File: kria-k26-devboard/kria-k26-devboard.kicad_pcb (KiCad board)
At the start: 8 copper layers, 121.5 x 89.8 mm, 397 parts, among them IC1 TPS2378DDA, IC2 USB5534B-5000JZX, J1 5-2337992-8, J2 USB4105-GF-A, J3 DC_SOCKET, J4 WE_68715014522, J5 47272-0001, J6 1140084168, J7 0878311420, J8 SSW-106-02-G-D-RA, M1 XILINX-KRIA-K26, P1 2199119-6, Q1 BSS138DW-7-F, Q2 PJA3441, Q3 BSS123, Q4 AO3401A, Q5 BSS138-7-F, Q6 BSS138-7-F, Q7 BSS138-7-F, Q8 BSS138-7-F, U1 DP83867CRRGZR, U10 AP62301WU-7, U11 AP62301WU-7, U12 LTC4358CDE, U13 LTC4358CDE, U14 LTC4358CDE, U15 USB3310C-CP, U16 TPD4E05U06QDQARQ1, U17 TPD4E05U06QDQARQ1, U18 GSB3112311HR, U19 TPD4E05U06QDQARQ1, U2 MAX5984AETI+T, U20 TPD4E05U06QDQARQ1, U21 GSB3112311HR, U22 PI4MSD5V9540BUEX, U23 FT4232HPQ, U24 SN74AVC4T245PWR, U25 FIN1019MTC, U26 TPD4E05U06QDQARQ1, U27 NVT4858HKZ, U28 TPS2116DRLR, U29 SN74AVC4T245PWR, U3 AP62301WU-7, U30 SN74AVC4T245PWR, U31 TPS3840PH30DBVR, U32 TPS3840PH30DBVR, U33 74LV07ATPWJ, U34 AP62301WU-7, U35 93LC56CT-IMC, U36 SN74AVC2T245RSWR, U37 SN74AVC2T245RSWR, U38 SN74AVC4T245PWR, U39 SN74AVC4T245PWR, U4 AP62301WU-7, U40 NC7WZ07P6X, U41 PCA9306D_118, U42 M24C64-FMC6TG, U43 TPD4E05U06QDQARQ1, U44 TPD4E05U06QDQARQ1, U5 AP62301WU-7, U6 AP62301WU-7, U7 AP62301WU-7, U8 RPX-4.0-R, U9 AP62301WU-7, Y1 ABM8G-25.000MHZ-18-D2Y-T, Y2 ABM8G-12.000MHZ-18-D2Y-T

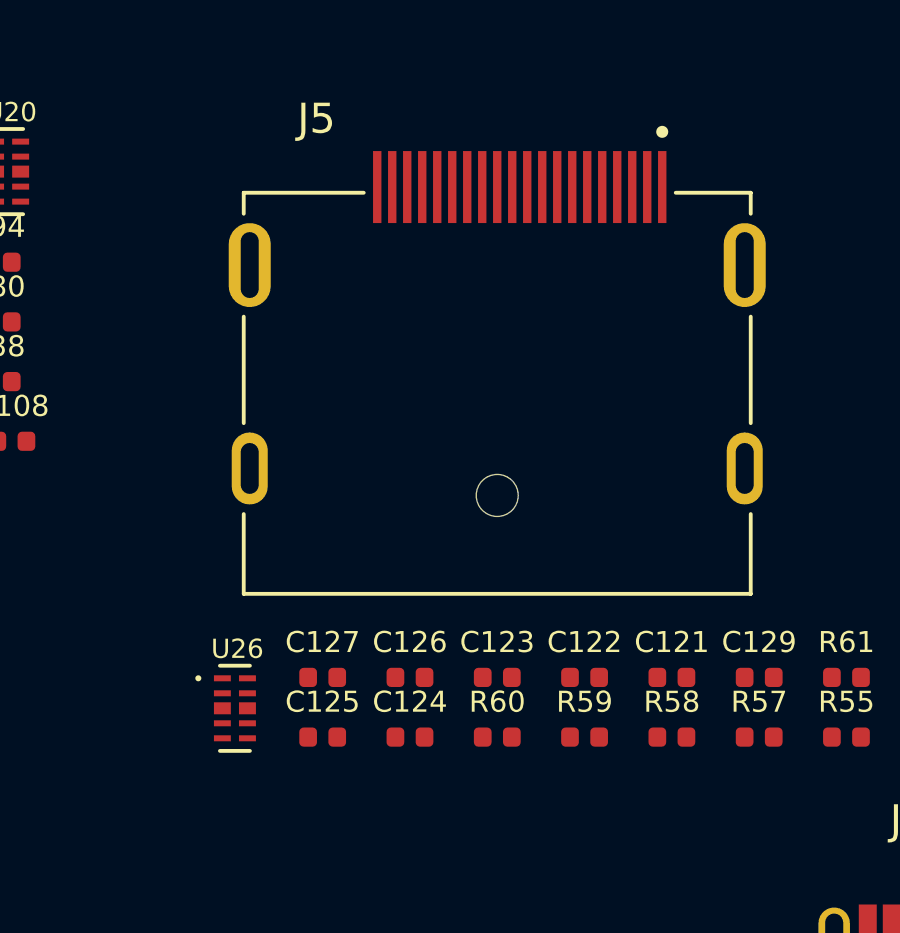
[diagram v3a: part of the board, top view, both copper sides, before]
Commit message: Added Led voltage indicator, fan circuit. Tidied up supply and SOM sheet
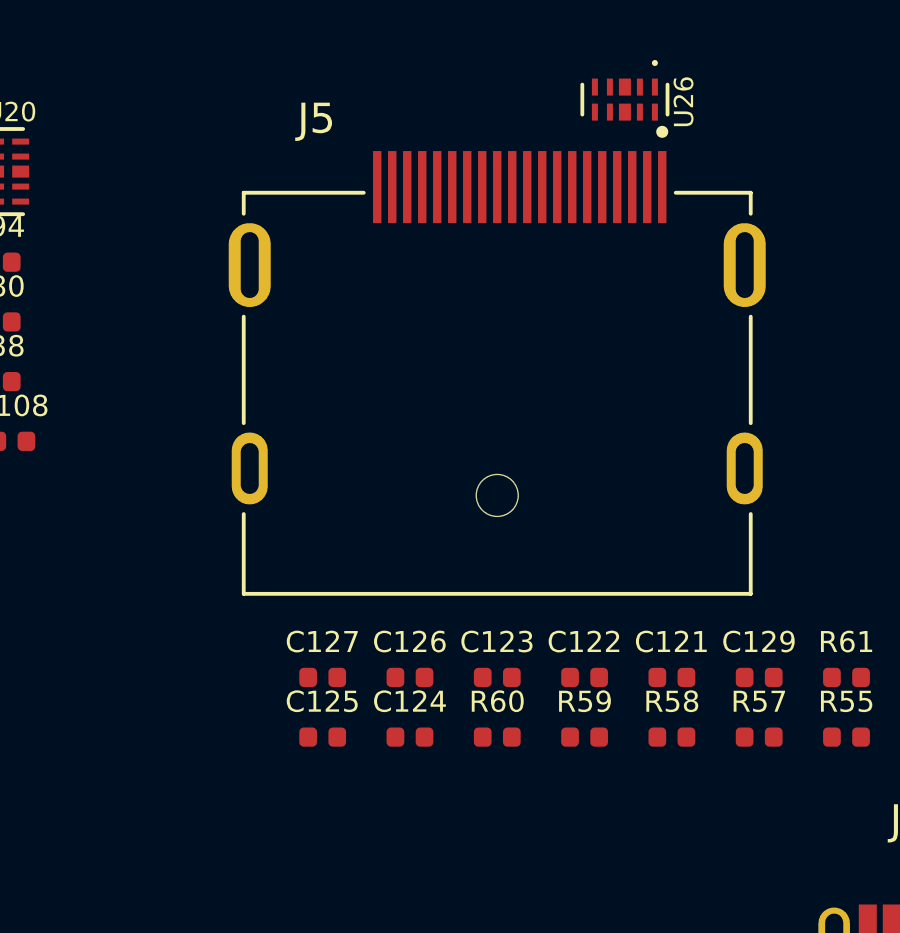
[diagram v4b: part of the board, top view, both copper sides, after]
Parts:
- moved U26 24.1 mm to (205.3, -118.8), turned to 270 degrees

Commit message: Initial placement of power supply
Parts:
- removed L9: PFL1609-102MEW, antmicro-footprints:0603-res
- added C197: C_100n_0402, antmicro-footprints:0402-cap, F.Cu at (44.7, 49.9)
- added C198: C_100n_0402, antmicro-footprints:0402-cap, F.Cu at (46.7, 52.9)
- added C199: C_100n_0402, antmicro-footprints:0402-cap, F.Cu at (100.2, -5.67)
- added C200: C_100n_0402, antmicro-footprints:0402-cap, F.Cu at (108.0, -17.6)
- added C201: C_100n_0402, antmicro-footprints:0402-cap, F.Cu at (183.9, -0.69)
- added C202: C_100n_0402, antmicro-footprints:0402-cap, F.Cu at (189.8, -10.8)
- added C203: C_10u_0603, antmicro-footprints:0603-cap, F.Cu at (191.3, -15.1)
- added C204: C_10u_0603, antmicro-footprints:0603-cap, F.Cu at (177.3, -1.47)
- added C205: C_22u_2220_100V, antmicro-footprints:2220-cap, F.Cu at (172.4, 84.1)
- added C206: C_22u_2220_100V, antmicro-footprints:2220-cap, F.Cu at (172.5, 77.3)
- added D18: LG_L29K-G2J1-24-Z, antmicro-footprints:LED_0603, F.Cu at (214.5, 85.0)
- added D19: LG_L29K-G2J1-24-Z, antmicro-footprints:LED_0603, F.Cu at (229.9, 95.0)
- added D20: LG_L29K-G2J1-24-Z, antmicro-footprints:LED_0603, F.Cu at (238.5, 93.9)
- added D21: LG_L29K-G2J1-24-Z, antmicro-footprints:LED_0603, F.Cu at (250.8, 93.3)
- added D22: LG_L29K-G2J1-24-Z, antmicro-footprints:LED_0603, F.Cu at (235.5, 115.9)
- added D23: LG_L29K-G2J1-24-Z, antmicro-footprints:LED_0603, F.Cu at (243.0, 107.6)
- added D24: 1N4148WS, antmicro-footprints:SOD-323F, F.Cu at (188.4, 70.5)
- added D25: 1N4148WS, antmicro-footprints:SOD-323F, F.Cu at (185.0, 70.5)
- added D26: LG_L29K-G2J1-24-Z, antmicro-footprints:LED_0603, F.Cu at (210.5, 97.9)
- added D27: LG_L29K-G2J1-24-Z, antmicro-footprints:LED_0603, F.Cu at (227.8, 128.4)
- added D28: LG_L29K-G2J1-24-Z, antmicro-footprints:LED_0603, F.Cu at (231.7, 125.9)
- added D6: 1N4148WS, antmicro-footprints:SOD-323F, F.Cu at (98.4, -8.12)
- added FB4: BLM15PD121SN1D, antmicro-footprints:0402-res, F.Cu at (54.4, -0.23)
- added FB5: BLM15PD121SN1D, antmicro-footprints:0402-res, F.Cu at (68.7, -16.2)
- added J10: BM08B-SRSS-TB-LF-SN, antmicro-footprints:BM08B-SRSS-TB-LF-SN, F.Cu at (89.1, -19.1)
- added J11: 10103594-0001LF, antmicro-footprints:USB_Micro_B_Female_10103594-0001LF, F.Cu at (157.7, -8.90)
- added J9: 22-23-2021, antmicro-footprints:PinHeader_1x2_P2.54mm_Drill1.02mm, F.Cu at (24.8, -7.25)
- added MP1: PCB_Mount_Hole_4.2_NPTH, antmicro-footprints:mounting-hole-4.2mm-NPTH, F.Cu at (77.0, 149.0)
- added MP2: PCB_Mount_Hole_4.2_NPTH, antmicro-footprints:mounting-hole-4.2mm-NPTH, F.Cu at (189.0, 149.0)
- added MP3: PCB_Mount_Hole_4.2_NPTH, antmicro-footprints:mounting-hole-4.2mm-NPTH, F.Cu at (189.0, 55.0)
- added MP4: PCB_Mount_Hole_4.2_NPTH, antmicro-footprints:mounting-hole-4.2mm-NPTH, F.Cu at (77.0, 55.0)
- added Q10: PJA3441, antmicro-footprints:SOT-23-3, F.Cu at (41.7, -1.67)
- added Q11: BSS138-7-F, antmicro-footprints:SOT-23-3, F.Cu at (37.0, -1.67)
- added Q12: BC847, antmicro-footprints:SOT-23-3, F.Cu at (210.7, 94.6)
- added Q13: BC847, antmicro-footprints:SOT-23-3, F.Cu at (216.8, 126.2)
- added Q14: BC847, antmicro-footprints:SOT-23-3, F.Cu at (221.5, 120.9)
- added Q15: PJA3441, antmicro-footprints:SOT-23-3, F.Cu at (149.9, 63.2)
- added Q16: BSS138-7-F, antmicro-footprints:SOT-23-3, F.Cu at (149.9, 66.7)
- added Q9: BSS138-7-F, antmicro-footprints:SOT-23-3, F.Cu at (46.4, 66.9)
- added R100: R_10k_0402, antmicro-footprints:0402-res, F.Cu at (103.1, -6.33)
- added R101: R_100k_0402, antmicro-footprints:0402-res, F.Cu at (68.7, -18.2)
- added R102: R_10k_0402, antmicro-footprints:0402-res, F.Cu at (113.8, -16.6)
- added R103: R_470R_0402, antmicro-footprints:0402-res, F.Cu at (24.3, 0.60)
- added R104: R_470R_0402, antmicro-footprints:0402-res, F.Cu at (61.9, -10.2)
- added R105: R_470R_0402, antmicro-footprints:0402-res, F.Cu at (59.0, -8.21)
- added R106: R_470R_0402, antmicro-footprints:0402-res, F.Cu at (59.0, -6.21)
- added R107: R_100k_0402, antmicro-footprints:0402-res, F.Cu at (109.4, -11.7)
- added R108: R_100k_0402, antmicro-footprints:0402-res, F.Cu at (112.3, -13.6)
- added R109: R_0R_0402, antmicro-footprints:0402-res, F.Cu at (107.7, -8.39)
- added R110: R_100k_0402, antmicro-footprints:0402-res, F.Cu at (106.0, -6.33)
- added R111: R_10k_0402, antmicro-footprints:0402-res, F.Cu at (106.5, -10.4)
- added R112: R_0R_0402, antmicro-footprints:0402-res, F.Cu at (189.7, -2.88)
- added R113: R_0R_0402, antmicro-footprints:0402-res, F.Cu at (192.6, -4.88)
- added R114: R_0R_0402, antmicro-footprints:0402-res, F.Cu at (186.9, -11.2)
- added R115: R_0R_0402, antmicro-footprints:0402-res, F.Cu at (194.8, -6.87)
- added R116: R_0R_0402, antmicro-footprints:0402-res, F.Cu at (186.9, 1.24)
- added R117: R_100k_0402, antmicro-footprints:0402-res, F.Cu at (195.6, -10.8)
- added R118: R_2k_0402, antmicro-footprints:0402-res, F.Cu at (214.6, 87.3)
- added R119: R_1k_0402, antmicro-footprints:0402-res, F.Cu at (229.5, 94.0)
- added R120: R_510R_0402, antmicro-footprints:0402-res, F.Cu at (236.2, 94.0)
- added R121: R_68_0402, antmicro-footprints:0402-res, F.Cu at (248.5, 93.4)
- added R122: R_10k_0402, antmicro-footprints:0402-res, F.Cu at (208.6, 95.9)
- added R123: R_1k_0402, antmicro-footprints:0402-res, F.Cu at (210.1, 96.9)
- added R124: R_10k_0402, antmicro-footprints:0402-res, F.Cu at (241.5, 125.0)
- added R125: R_1k_0402, antmicro-footprints:0402-res, F.Cu at (242.7, 120.6)
- added R126: R_1k_0402, antmicro-footprints:0402-res, F.Cu at (251.8, 113.8)
- added R127: R_68_0402, antmicro-footprints:0402-res, F.Cu at (245.6, 120.7)
- added R128: R_10k_0402, antmicro-footprints:0402-res, F.Cu at (238.6, 128.0)
- added R129: R_1k_0402, antmicro-footprints:0402-res, F.Cu at (248.9, 116.7)
- added R130: R_100k_0402, antmicro-footprints:0402-res, F.Cu at (152.2, 63.4)
- added R98: R_100R_0402, antmicro-footprints:0402-res, F.Cu at (44.7, 52.9)
- added R99: R_100R_0402, antmicro-footprints:0402-res, F.Cu at (42.7, 50.7)
- added U45: SN65LVDS1DR, antmicro-footprints:SOIC-8_W3.9mm, F.Cu at (39.6, 58.3)
- added U46: XLL736027.000000X, antmicro-footprints:Oscillator_SMD_IDT_JU6-6_7.0x5.0mm_P2.54mm, F.Cu at (39.7, 65.4)
- added U47: MCP1799-3302H_DB, antmicro-footprints:SOT-223, F.Cu at (156.5, -1.66)
- added U48: MCP1799-3302H_DB, antmicro-footprints:SOT-223, F.Cu at (166.9, -6.22)
- added Y3: ECS-2520MVLC-260-CM-TR, antmicro-footprints:Oscillator_SMD_ECS_2520MV-xxx-xx-4Pin_2.5x2.0mm, F.Cu at (37.6, 53.2)
- added Y4: AX3DAF1-125.0000, antmicro-footprints:AX3DAF1, F.Cu at (45.9, 59.4)
- added Y5: SIT9120AI-2C3-33E100.000000X, antmicro-footprints:SiTime_5.0x3.2, F.Cu at (39.8, 72.6)
- C158: value C_10u_25V_0603 -> C_100n_0402; footprint antmicro-footprints:0603-cap -> antmicro-footprints:0402-cap
- C175: value C_10u_0603 -> C_100n_0402; footprint antmicro-footprints:0603-cap -> antmicro-footprints:0402-cap
- C177: value C_4u7_0402 -> C_1u_1210_100V; footprint antmicro-footprints:0402-cap -> antmicro-footprints:1210-cap
- C25, C27: value C_100n_0805_100V -> C_100n_0402; footprint antmicro-footprints:0805-cap -> antmicro-footprints:0402-cap
- C28: value C_47u_ELEC_100V -> C_100n_0402; footprint antmicro-footprints:CP_Elec_10x10.5 -> antmicro-footprints:0402-cap
- C29: value C_1n0_0402 -> C_100n_0402
- C30, C31: value C_47u_ELEC_100V -> C_22u_2220_100V; footprint antmicro-footprints:CP_Elec_10x10.5 -> antmicro-footprints:2220-cap
- D17: value PMEG3010CEJ -> 1N4148WS
- D3: value 1N4448WS -> PTVS5V0Z1USKPYL; footprint Diode_SMD:D_SOD-323 -> antmicro-footprints:SOD-964
- D5: value SMAJ58A-13-F -> 1N4148WS; footprint antmicro-footprints:DO-214AC -> antmicro-footprints:SOD-323F
- P1: moved to B.Cu
- Q2: value PJA3441 -> BSS138-7-F
- R12: value R_2M2_0805 -> R_100R_0402; footprint antmicro-footprints:0805-res -> antmicro-footprints:0402-res
- R15: value R_0R_0402 -> R_100R_0402
- R16: value R_100k_0805 -> R_100R_0402; footprint antmicro-footprints:0805-res -> antmicro-footprints:0402-res
- R70: value R_10k_0402 -> R_1M0_0402
- R74: value R_33k2_0402 -> R_10k_0402
- R75: value R_10k_0402 -> R_100R_0402
- R89: value R_100k_0402 -> R_2k49_0402
- R93: value R_10k_0402 -> R_100k_0402
- U2: value MAX5984AETI+T -> SI53152-A01AGMR; footprint antmicro-footprints:Maxim_MAX5984_TQFN-EP-28 -> antmicro-footprints:SIL_QFN24_4X4
- U30: value SN74AVC4T245PWR -> SN74AVC2T245RSWR; footprint Package_SO:TSSOP-16_4.4x5mm_P0.65mm -> antmicro-footprints:Texas_RSW0010A
- U34: value AP62301WU-7 -> SN74LVC1G125DBVR; footprint antmicro-footprints:TSOT23-6 -> antmicro-footprints:SOT-753
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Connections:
- net /Camera interfaces/CCI0_I2C_SCL_3V3 renamed /Camera interface/CCI0_I2C_SCL_3V3
- net /Camera interfaces/CCI0_I2C_SDA_3V3 renamed /Camera interface/CCI0_I2C_SDA_3V3
- net /Camera interfaces/CCI1_I2C_SCL_3V3 renamed /Camera interface/CCI1_I2C_SCL_3V3
- net /Camera interfaces/CCI1_I2C_SDA_3V3 renamed /Camera interface/CCI1_I2C_SDA_3V3
- net /Camera interfaces/HDA01 renamed /Camera interface/HDA01
- net /Camera interfaces/HPA00_CC_N renamed /Camera interface/HPA00_CC_N
- net /Camera interfaces/HPA00_CC_P renamed /Camera interface/HPA00_CC_P
- net /Camera interfaces/HPA01_N renamed /Camera interface/HPA01_N
- net /Camera interfaces/HPA01_P renamed /Camera interface/HPA01_P
- net /Camera interfaces/HPA02_N renamed /Camera interface/HPA02_N
- net /Camera interfaces/HPA02_P renamed /Camera interface/HPA02_P
- net /Camera interfaces/HPA03_N renamed /Camera interface/HPA03_N
- net /Camera interfaces/HPA03_P renamed /Camera interface/HPA03_P
- net /Camera interfaces/HPA04_N renamed /Camera interface/HPA04_N
- net /Camera interfaces/HPA04_P renamed /Camera interface/HPA04_P
- net /Camera interfaces/HPA05_CC_N renamed /Camera interface/HPA05_CC_N
- net /Camera interfaces/HPA05_CC_P renamed /Camera interface/HPA05_CC_P
- net /Camera interfaces/HPA06_N renamed /Camera interface/HPA06_N
- net /Camera interfaces/HPA06_P renamed /Camera interface/HPA06_P
- net /Camera interfaces/HPA07_N renamed /Camera interface/HPA07_N
- net /Camera interfaces/HPA07_P renamed /Camera interface/HPA07_P
- net /Camera interfaces/HPA08_N renamed /Camera interface/HPA08_N
- net /Camera interfaces/HPA08_P renamed /Camera interface/HPA08_P
- net /Camera interfaces/HPA09_N renamed /Camera interface/HPA09_N
- net /Camera interfaces/HPA09_P renamed /Camera interface/HPA09_P
- net /Debug and JTAG/EEPROM_WC renamed /Debug and JTAG/~EEPROM_WC
- net /Debug and JTAG/PC4_CON_PGND renamed /Debug and JTAG/CONN_GND
- net /Debug and JTAG/PD_CC1 renamed /Debug and JTAG/USBC_CC1
- net /Debug and JTAG/PD_CC2 renamed /Debug and JTAG/USBC_CC2
- net /Ethernet/ETH_RESET renamed /Ethernet/~ETH_RESET
- net /PCIE M2 key E /M2_PEWAKE# renamed /PCIE M2 key E /~M2_PEWAKE
- net /Reset logic/SD_CARD_RESET renamed /Reset logic/~SD_CARD_RESET
- net /Reset logic/USB_HUB_RESET renamed /Reset logic/~USB_HUB_RESET
- net /Reset logic/USB_PHY_RESET renamed /Reset logic/~USB_PHY_RESET
- net Net-(R77-Pad1) renamed /Debug and JTAG/EEDATA
- net Net-(R78-Pad2) renamed /Debug and JTAG/EECLK
- net Net-(R79-Pad2) renamed /Debug and JTAG/EECS
- C142 pad 1: /SD 3.0 card/VCCB -> PS_3V3
- C148 pad 1: PS_1V8 -> PS_3V3
- C152 pad 1: PS_3V3 -> PL_3V3
- C156 pad 1: PS_3V3 -> PL_3V3
- C157 pad 2: /Debug and JTAG/USB_3V45 -> /Debug and JTAG/USB_3V3
- C158 pad 1: VBUS -> PS_3V3
- C159 pad 2: /Debug and JTAG/USB_3V45 -> /Debug and JTAG/USB_3V3
- C161 pad 2: /Debug and JTAG/USB_3V45 -> /Debug and JTAG/USB_3V3
- C163 pad 2: /Debug and JTAG/USB_3V45 -> /Debug and JTAG/USB_3V3
- C165 pad 2: /Debug and JTAG/USB_3V45 -> /Debug and JTAG/USB_3V3
- C169 pad 1: /Debug and JTAG/USB_3V45 -> /Debug and JTAG/USB_3V3
- C172 pad 1: /Debug and JTAG/USB_3V45 -> /Debug and JTAG/USB_3V3
- C173 pad 1: Net-(C173-Pad1) -> PS_3V3
- C173 pad 2: Net-(C173-Pad2) -> GND
- C175 pad 1: /Debug and JTAG/USB_3V45 -> PS_3V3
- C177 pad 1: /Debug and JTAG/USB_3V3 -> Net-(C177-Pad1)
- C179 pad 1: /Debug and JTAG/USB_3V45 -> /Debug and JTAG/USB_3V3
- C180 pad 1: /Debug and JTAG/USB_3V45 -> /Debug and JTAG/USB_3V3
- C181 pad 1: /Debug and JTAG/USB_3V45 -> /Debug and JTAG/USB_3V3
- C182 pad 1: /Debug and JTAG/USB_3V45 -> /Debug and JTAG/USB_3V3
- C183 pad 1: /Debug and JTAG/USB_3V45 -> /Debug and JTAG/USB_3V3
- C187 pad 1: /Debug and JTAG/USB_3V45 -> /Debug and JTAG/USB_3V3
- C25 pad 1: /Power Supply/PoE/VDD_POE_OUT -> PS_1V8
- C25 pad 2: /Power Supply/PoE/VSS_POE_OUT -> GND
- C27 pad 1: /Power Supply/PoE/VDD_POE_OUT -> /SD 3.0 card/VCCB
- C27 pad 2: /Power Supply/PoE/VSS_POE_IN -> GND
- C28 pad 1: /Power Supply/PoE/VDD_POE_OUT -> PS_3V3
- C28 pad 2: /Power Supply/PoE/VSS_POE_IN -> GND
- C29 pad 1: Net-(C29-Pad1) -> PS_3V3
- C29 pad 2: /Power Supply/PoE/VSS_POE_IN -> GND
- C45 pad 2: Net-(C45-Pad2) -> GND
- C56 pad 2: Net-(C45-Pad2) -> GND
- C60 pad 2: Net-(C60-Pad2) -> GND
- C61 pad 2: Net-(C60-Pad2) -> GND
- D1 pad 3: Net-(D1-Pad3) -> /Ethernet/POE_VC1
- D1 pad 4: Net-(D1-Pad4) -> /Ethernet/POE_VC2
- D17 pad A: /Debug and JTAG/USB_3V45 -> Net-(D17-PadA)
- D17 pad K: /Debug and JTAG/USB_3V3 -> Net-(D17-PadK)
- D2 pad 3: Net-(D2-Pad3) -> /Ethernet/POE_VC3
- D2 pad 4: Net-(D2-Pad4) -> /Ethernet/POE_VC4
- D5 pad A: /Power Supply/PoE/VSS_POE_OUT -> GND
- D5 pad K: /Power Supply/PoE/VDD_POE_OUT -> Net-(C177-Pad1)
- D7 pad 1: /Power Supply/USB-C socket/PD_CC1 -> /Power Supply/USB-C socket/USBC_CC1
- D7 pad 2: /Power Supply/USB-C socket/PD_CC1 -> /Power Supply/USB-C socket/USBC_CC2
- D8 pad 1: /Debug and JTAG/DBG_USB_N -> /Debug and JTAG/USBC_N
- D8 pad 2: /Debug and JTAG/DBG_USB_P -> /Debug and JTAG/USBC_P
- FB1 pad 1: /Debug and JTAG/USB_3V3 -> /Debug and JTAG/PD_3V3
- FB3 pad 1: /Debug and JTAG/USB_3V45 -> /Debug and JTAG/USB_3V3
- J1 pad 11: Net-(J1-Pad11) -> /Ethernet/POE_VC1
- J1 pad 12: Net-(J1-Pad12) -> /Ethernet/POE_VC2
- J1 pad 13: Net-(J1-Pad13) -> /Ethernet/POE_VC3
- J1 pad 14: Net-(J1-Pad14) -> /Ethernet/POE_VC4
- J2 pad A5: /Power Supply/USB-C socket/PD_CC1 -> /Power Supply/USB-C socket/USBC_CC1
- J2 pad A6: /Debug and JTAG/DBG_USB_P -> /Debug and JTAG/USBC_P
- J2 pad A7: /Debug and JTAG/DBG_USB_N -> /Debug and JTAG/USBC_N
- J2 pad B5: /Power Supply/USB-C socket/PD_CC1 -> /Power Supply/USB-C socket/USBC_CC2
- J2 pad B6: /Debug and JTAG/DBG_USB_P -> /Debug and JTAG/USBC_P
- J2 pad B7: /Debug and JTAG/DBG_USB_N -> /Debug and JTAG/USBC_N
- J4 pad 32: /Camera interfaces/CAM0_PWDN -> /Camera interface/CAM0_VSYNC
- J4 pad 33: /Camera interfaces/CAM0_RST -> /Camera interface/CAM0_RST
- J4 pad 34: /Camera interfaces/CAM1_PWDN -> /Camera interface/CAM1_VSYNC
- J7 pad 4: Net-(J7-Pad4) -> /Debug and JTAG/JTAG_TMS_C2M
- J_SOM240_1 pad A15: /Reset logic/HDA09 -> /Camera interface/CAM1_VSYNC
- J_SOM240_1 pad A34: /Xilinx K26 SOM/MIO41 -> /Reset logic/MIO41
- J_SOM240_1 pad B17: /Reset logic/HDA04 -> /Camera interface/CAM0_VSYNC
- J_SOM240_1 pad B49: /Xilinx K26 SOM/REFCLK1_C2M_P -> /Clock distribution/GTR_REFCLK1_C2M_P
- J_SOM240_1 pad B50: /Xilinx K26 SOM/REFCLK1_C2M_N -> /Clock distribution/GTR_REFCLK1_C2M_N
- J_SOM240_1 pad C16: /Xilinx K26 SOM/PS_SRST_C2M_L -> /Debug and JTAG/~PS_SRST_C2M
- J_SOM240_1 pad C47: /Xilinx K26 SOM/GTR_REFCLK0_C2M_P -> /Clock distribution/GTR_REFCLK0_C2M_P
- J_SOM240_1 pad C48: /Xilinx K26 SOM/GTR_REFCLK0_C2M_N -> /Clock distribution/GTR_REFCLK0_C2M_N
- J_SOM240_1 pad D53: /Xilinx K26 SOM/GTR_REFCLK2_C2M_P -> /Clock distribution/GTR_REFCLK2_C2M_P
- J_SOM240_1 pad D54: /Xilinx K26 SOM/GTR_REFCLK2_C2M_N -> /Clock distribution/GTR_REFCLK2_C2M_N
- P1 pad 52: /PCIE M2 key E /M2_PERST# -> /PCIE M2 key E /~M2_PERST
- P1 pad 53: /PCIE M2 key E /M2_CLKREQ# -> /Clock distribution/~M2_CLKREQ
- Q2 pad 1: /Power Supply/PoE/POE_ACTIVE -> /Reset logic/PS_RST
- Q2 pad 2: /Power Supply/PoE/VDD_POE_OUT -> GND
- Q2 pad 3: /Power Supply/PoE/VDD_POE_IN -> /Clock distribution/PS_CLK_EN
- Q4 pad 2: Net-(C143-Pad1) -> PS_3V3
- Q4 pad 3: PS_3V3 -> Net-(C143-Pad1)
- R12 pad 1: /Power Supply/PoE/VDD_POE_OUT -> /Clock distribution/GTR_REFCLK3_P
- R12 pad 2: /Power Supply/PoE/VSS_POE_OUT -> /Clock distribution/GTR_REFCLK3_N
- R15 pad 1: Net-(R15-Pad1) -> /Clock distribution/GTR_REFCLK3_C2M_P
- R15 pad 2: /Power Supply/PoE/VSS_POE_IN -> /Clock distribution/GTR_REFCLK3_C2M_N
- R16 pad 1: /Power Supply/PoE/VDD_POE_IN -> /Clock distribution/GTR_REFCLK0_C2M_P
- R16 pad 2: /Power Supply/PoE/POE_ACTIVE -> /Clock distribution/GTR_REFCLK0_C2M_N
- R28 pad 2: Net-(C60-Pad2) -> GND
- R48 pad 2: /PCIE M2 key E /M2_CLKREQ# -> /Clock distribution/~M2_CLKREQ
- R50 pad 2: /PCIE M2 key E /M2_PERST# -> /PCIE M2 key E /~M2_PERST
- R70 pad 1: PL_3V3 -> GND
- R70 pad 2: /Camera interfaces/CAM0_RST -> /Clock distribution/~M2_CLKREQ
- R74 pad 1: /Debug and JTAG/USB_3V45 -> PS_3V3
- R74 pad 2: Net-(R74-Pad2) -> Net-(Q9-Pad3)
- R75 pad 1: Net-(R74-Pad2) -> Net-(R75-Pad1)
- R75 pad 2: GND -> Net-(R75-Pad2)
- R76 pad 1: /Debug and JTAG/USB_3V45 -> /Debug and JTAG/USB_3V3
- R78 pad 1: /Debug and JTAG/USB_3V45 -> /Debug and JTAG/USB_3V3
- R79 pad 1: /Debug and JTAG/USB_3V45 -> /Debug and JTAG/USB_3V3
- R81 pad 1: /Debug and JTAG/3V45 -> /Debug and JTAG/USB_3V3
- R82 pad 1: /Debug and JTAG/USB_3V45 -> /Debug and JTAG/USB_3V3
- R83 pad 1: /Debug and JTAG/FTDI_EEPROM_WC -> PS_1V8
- R83 pad 2: GND -> /Ethernet/MIO71
- R84 pad 1: /Debug and JTAG/USB_3V45 -> /Debug and JTAG/USB_3V3
- R85 pad 1: /Debug and JTAG/USB_3V45 -> /Debug and JTAG/USB_3V3
- R86 pad 1: /Debug and JTAG/USB_3V45 -> /Debug and JTAG/USB_3V3
- R87 pad 1: /Debug and JTAG/USB_3V45 -> /Debug and JTAG/USB_3V3
- R88 pad 1: PS_3V3 -> GND
- R89 pad 1: PS_3V3 -> /Ethernet/MIO71
- R89 pad 2: Net-(R89-Pad2) -> GND
- R90 pad 1: PS_3V3 -> GND
- R91 pad 1: PS_3V3 -> GND
- R92 pad 1: PS_3V3 -> GND
- R93 pad 1: /Reset logic/PS_RST -> 5V_SOM
- R93 pad 2: GND -> Net-(Q10-Pad1)
- S1 pad 2: Net-(S1-Pad2) -> Net-(D17-PadK)
- S1 pad 4: Net-(S1-Pad2) -> Net-(D17-PadK)
- U10 pad 5: /Power Supply/VCCOEN_PL_M2C -> /Power Supply/VCCOEN_PS_M2C
- U11 pad 5: /Power Supply/VCCOEN_PL_M2C -> /Power Supply/VCCOEN_PS_M2C
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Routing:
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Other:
- board size 121.5 x 89.8 mm -> 118 x 100 mm
- net class Default: clearance 0.076 -> 0.125; trace_width 0.076 -> 0.125; via_dia 0.8 -> 0.55; via_drill 0.4 -> 0.3
- rule trace_clearance: 0.076 -> 0.125
- rule trace_min: 0.076 -> 0.125
- rule via_min_drill: 0.2 -> 0.15

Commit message: Progress in PCB placement
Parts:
- removed the C121 at (128.6, 33.6)
- removed the C122 at (142.5, 18.7)
- removed the C123 at (111.1, 33.6)
- removed the C130 at (46.5, -2.69)
- removed the C15 at (226.5, -15.5)
- removed the C16 at (223.7, -1.40)
- removed the C17 at (233.6, -18.0)
- removed the C32 at (168.2, 116.0)
- removed the C33 at (168.2, 118.0)
- removed the C35 at (227.4, 100.2)
- removed the C40 at (229.5, 96.1)
- removed the C43 at (210.1, 98.9)
- removed the C46 at (226.9, 95.2)
- removed the C49 at (207.5, 98.0)
- removed the C51 at (228.0, 95.2)
- removed the C54 at (208.6, 98.0)
- removed the C56 at (219.1, 82.1)
- removed the C57 at (225.8, 86.3)
- removed the C59 at (246.9, 86.4)
- removed the C6 at (226.5, -13.5)
- removed the C62 at (230.0, 83.7)
- removed the C64 at (251.1, 83.7)
- removed the C65 at (225.8, 83.5)
- removed the C67 at (246.9, 83.6)
- removed the C68 at (224.7, 83.5)
- removed the C70 at (245.8, 83.6)
- removed the C72 at (170.6, 120.1)
- removed the C79 at (63.2, 45.2)
- removed the C81 at (67.6, 40.3)
- removed the D19 at (229.9, 95.0)
- removed the D26 at (210.5, 97.9)
- removed the D28 at (231.7, 125.9)
- removed the IC2 at (79.8, 19.8)
- removed the J11 at (157.7, -8.90)
- removed the J4 at (80.5, 105.4)
- removed the J6 at (133.7, 145.0)
- removed the R118 at (214.6, 87.3)
- removed the R126 at (251.8, 113.8)
- removed the R129 at (248.9, 116.7)
- removed the R18 at (244.4, 124.7)
- removed the R23 at (235.7, 128.0)
- removed the R24 at (253.5, 111.8)
- removed the R27 at (221.4, 87.4)
- removed the R28 at (221.4, 85.5)
- removed the R29 at (230.8, 86.5)
- removed the R30 at (230.3, 87.9)
- removed the R4 at (239.4, -18.0)
- removed the R44 at (52.2, 127.9)
- removed the R46 at (50.2, 127.9)
- removed the R47 at (40.0, 99.6)
- removed the R60 at (142.5, 20.7)
- removed the R64 at (144.9, 168.9)
- removed the R8 at (224.4, -5.45)
- removed the U10 at (238.8, 86.0)
- removed the U11 at (249.5, 86.1)
- removed the U15 at (44.2, 38.4)
- removed the U24 at (136.6, 16.0)
- removed the U25 at (136.6, 22.6)
- removed the U3 at (228.3, 98.1)
- removed the U6 at (209.0, 100.9)
- removed the U8 at (218.0, 85.5)
- removed the U9 at (228.3, 86.0)
- added C104: C_47u_0805, antmicro-footprints:0805-cap, F.Cu at (46.5, -2.69)
- added C162: C_47u_16V_1206, antmicro-footprints:1206-cap, F.Cu at (167.3, 115.7)
- added C163: C_47u_16V_1206, antmicro-footprints:1206-cap, F.Cu at (167.3, 117.7)
- added C165: C_10u_25V_0603, antmicro-footprints:0603-cap, F.Cu at (174.2, 114.9)
- added C166: C_10u_25V_0603, antmicro-footprints:0603-cap, F.Cu at (176.6, 114.9)
- added C169: C_10u_25V_0603, antmicro-footprints:0603-cap, F.Cu at (186.7, 121.2)
- added C174: C_100n_0402, antmicro-footprints:0402-cap, F.Cu at (188.7, 117.1)
- added C177: C_100n_0402, antmicro-footprints:0402-cap, F.Cu at (188.6, 126.7)
- added C179: C_22u_0603, antmicro-footprints:0603-cap, F.Cu at (186.2, 116.2)
- added C182: C_22u_0603, antmicro-footprints:0603-cap, F.Cu at (185.9, 125.8)
- added C184: C_22u_0603, antmicro-footprints:0603-cap, F.Cu at (187.3, 116.2)
- added C187: C_22u_0603, antmicro-footprints:0603-cap, F.Cu at (187.1, 125.8)
- added C189: C_10u_25V_0603, antmicro-footprints:0603-cap, F.Cu at (173.4, 136.9)
- added C191: C_10u_25V_0603, antmicro-footprints:0603-cap, F.Cu at (185.3, 145.2)
- added C192: C_100n_0402, antmicro-footprints:0402-cap, F.Cu at (177.7, 134.3)
- added C194: C_100n_0402, antmicro-footprints:0402-cap, F.Cu at (182.7, 140.9)
- added C195: C_22u_0603, antmicro-footprints:0603-cap, F.Cu at (173.4, 134.2)
- added C197: C_22u_0603, antmicro-footprints:0603-cap, F.Cu at (182.6, 145.2)
- added C198: C_22u_0603, antmicro-footprints:0603-cap, F.Cu at (172.3, 134.2)
- added C200: C_22u_0603, antmicro-footprints:0603-cap, F.Cu at (182.6, 146.2)
- added C202: C_100n_0402, antmicro-footprints:0402-cap, F.Cu at (169.7, 119.8)
- added C47: C_100n_0402, antmicro-footprints:0402-cap, B.Cu at (95.5, 78.8)
- added C7: C_100n_0402, antmicro-footprints:0402-cap, F.Cu at (130.2, 92.7)
- added C85: C_1u_0402, antmicro-footprints:0402-cap, B.Cu at (149.0, 82.8)
- added C87: C_1u_0402, antmicro-footprints:0402-cap, B.Cu at (148.2, 77.0)
- added C9: C_100n_0402, antmicro-footprints:0402-cap, F.Cu at (129.6, 74.7)
- added C94: C_100n_0402, antmicro-footprints:0402-cap, F.Cu at (149.8, 75.0)
- added C95: C_100n_0402, antmicro-footprints:0402-cap, F.Cu at (144.6, 82.7)
- added C96: C_100n_0402, antmicro-footprints:0402-cap, F.Cu at (149.9, 85.0)
- added D14: LG_L29K-G2J1-24-Z, antmicro-footprints:LED_0603, F.Cu at (172.0, 117.8)
- added D15: LG_L29K-G2J1-24-Z, antmicro-footprints:LED_0603, F.Cu at (189.2, 116.0)
- added D20: LG_L29K-G2J1-24-Z, antmicro-footprints:LED_0603, F.Cu at (176.7, 132.4)
- added IC1: USB5534B-5000JZX, antmicro-footprints:USB5534B-5000JZX, F.Cu at (100.5, 78.0)
- added J2: 1140084168, antmicro-footprints:MicroSD_1140084168, F.Cu at (130.9, 145.3)
- added J3: WE_68715014522, antmicro-footprints:WE_68715014522, F.Cu at (80.5, 105.4)
- added J8: 1050170001, antmicro-footprints:USB_Micro_B_Female_1050170001, F.Cu at (145.5, 146.9)
- added N2: antmicro_logo, antmicro-footprints:antmicro-logo_scaled_15mm, F.Cu at (89.5, 149.4)
- added R100: R_10k_0402, antmicro-footprints:0402-res, F.Cu at (178.9, 120.2)
- added R101: R_2k49_0402, antmicro-footprints:0402-res, F.Cu at (178.9, 118.3)
- added R102: R_1k_0402, antmicro-footprints:0402-res, F.Cu at (188.8, 115.0)
- added R105: R_33R_0402, antmicro-footprints:0402-res, F.Cu at (88.0, 115.4)
- added R106: R_1k_0402, antmicro-footprints:0402-res, F.Cu at (188.6, 124.7)
- added R107: R_31k6_0402, antmicro-footprints:0402-res, F.Cu at (190.1, 119.7)
- added R108: R_10k_0402, antmicro-footprints:0402-res, F.Cu at (189.6, 121.0)
- added R113: R_4k99_0402, antmicro-footprints:0402-res, F.Cu at (189.9, 129.2)
- added R114: R_10k_0402, antmicro-footprints:0402-res, F.Cu at (189.4, 130.6)
- added R117: R_33R_0402, antmicro-footprints:0402-res, F.Cu at (88.0, 113.5)
- added R121: R_33R_0402, antmicro-footprints:0402-res, F.Cu at (88.0, 112.7)
- added R127: R_4k99_0402, antmicro-footprints:0402-res, F.Cu at (185.6, 139.9)
- added R13: R_100k_0402, antmicro-footprints:0402-res, F.Cu at (137.0, 68.4)
- added R31: R_2k2_0402, antmicro-footprints:0402-res, F.Cu at (82.2, 112.5)
- added R49: R_2k2_0402, antmicro-footprints:0402-res, F.Cu at (154.7, 79.1)
- added R53: R_4k7_0402, antmicro-footprints:0402-res, F.Cu at (142.7, 81.6)
- added R99: R_2k_0402, antmicro-footprints:0402-res, F.Cu at (172.1, 120.1)
- added U1: SN74AVC4T245PWR, antmicro-footprints:TSSOP-16_4.4x5mm_P0.65mm, F.Cu at (132.0, 88.5)
- added U14: USB3310C-CP, antmicro-footprints:Microchip_QFN24_4X4, F.Cu at (51.0, 74.5)
- added U2: FIN1019MTC, antmicro-footprints:TSSOP-14_4.4x5mm_P0.65mm, F.Cu at (132.1, 78.8)
- added U37: RPX-4.0-R, antmicro-footprints:Recom_15-PowerBQFN, F.Cu at (175.5, 118.3)
- added U38: AP62301WU-7, antmicro-footprints:TSOT23-6, F.Cu at (187.6, 119.2)
- added U41: AP62301WU-7, antmicro-footprints:TSOT23-6, F.Cu at (187.4, 128.7)
- added U44: AP62301WU-7, antmicro-footprints:TSOT23-6, F.Cu at (183.7, 137.0)
- added U45: AP62301WU-7, antmicro-footprints:TSOT23-6, F.Cu at (185.1, 142.6)
- added U46: LTC4358CDE, antmicro-footprints:Linear_DFN-14, F.Cu at (166.5, 120.9)
- C100: renamed from C21; moved to B.Cu
- C101: renamed from C22; moved to B.Cu
- C102: renamed from C23; moved to B.Cu
- C103: renamed from C24; moved to B.Cu
- C21: renamed from C146; moved to B.Cu
- C22: renamed from C147; moved to B.Cu
- C23: renamed from C143; moved to B.Cu
- C24: renamed from C144; moved to B.Cu
- C43: renamed from C77; moved to B.Cu
- C44: renamed from C78; moved to B.Cu
- C45: value C_10u_25V_0603 -> C_100n_0402; footprint antmicro-footprints:0603-cap -> antmicro-footprints:0402-cap; moved to B.Cu
- C46: renamed from C80; moved to B.Cu
- C48: renamed from C82; moved to B.Cu
- C49: renamed from C83; moved to B.Cu
- C50: renamed from C84; moved to B.Cu
- C51: renamed from C85; moved to B.Cu
- C52: renamed from C86; moved to B.Cu
- C54: renamed from C88; moved to B.Cu
- C57: renamed from C91; moved to B.Cu
- C59: renamed from C93; moved to B.Cu
- C60: renamed from C94; moved to B.Cu
- C8: value C_1u_0402 -> C_100n_0402
- C80: renamed from C1; moved to B.Cu
- C81: renamed from C2; moved to B.Cu
- C82: renamed from C3; moved to B.Cu
- C83: renamed from C4; moved to B.Cu
- C84: renamed from C5; moved to B.Cu
- C86: renamed from C7; moved to B.Cu
- C88: renamed from C9; moved to B.Cu
- C98: renamed from C19; moved to B.Cu
- C99: renamed from C20; moved to B.Cu
- MP1, MP2, MP3, MP4: value PCB_Mount_Hole_4.2_NPTH -> PCB_Mount_Hole_3mm_6mm_pad; footprint antmicro-footprints:mounting-hole-4.2mm-NPTH -> antmicro-footprints:mounting-hole-3.2mm
- Q1: renamed from Q3; moved to B.Cu
- Q12, Q13, Q14: value BC847 -> DTC014TEBTL; footprint antmicro-footprints:SOT-23-3 -> antmicro-footprints:SOT-416
- Q2: renamed from Q4; moved to B.Cu
- R122: value R_10k_0402 -> R_1k_0402
- R123: value R_1k_0402 -> R_31k6_0402
- R17: value R_31k6_0402 -> R_33R_0402
- R18: renamed from R3; moved to B.Cu
- R19: renamed from R66; moved to B.Cu
- R33: value R_4k99_0402 -> R_2k2_0402
- R34: value R_10k_0402 -> R_2k2_0402
- SP1: moved to B.Cu
- U12: value LTC4358CDE -> TPD4E05U06QDQARQ1; footprint antmicro-footprints:Linear_DFN-14 -> antmicro-footprints:TPD4E05U06QDQARQ1; moved to B.Cu
- U24: renamed from U29; footprint Package_SO:TSSOP-16_4.4x5mm_P0.65mm -> antmicro-footprints:TSSOP-16_4.4x5mm_P0.65mm
- U32: renamed from U38; footprint Package_SO:TSSOP-16_4.4x5mm_P0.65mm -> antmicro-footprints:TSSOP-16_4.4x5mm_P0.65mm
- U33: renamed from U39; footprint Package_SO:TSSOP-16_4.4x5mm_P0.65mm -> antmicro-footprints:TSSOP-16_4.4x5mm_P0.65mm
- U43: value TPD4E05U06QDQARQ1 -> AP62301WU-7; footprint antmicro-footprints:TPD4E05U06QDQARQ1 -> antmicro-footprints:TSOT23-6
- moved C115 204.3 mm to (153.9, 190.6)
- moved C117 204.3 mm to (169.3, 175.7)
- moved C118 204.3 mm to (148.1, 190.7)
- moved C120 204.3 mm to (151.0, 190.7)
- moved C122 204.3 mm to (156.8, 190.6)
- moved C123 204.3 mm to (164.6, 178.7)
- moved C124 204.3 mm to (170.4, 177.7)
- moved D9 204.3 mm to (155.0, 188.2)
- moved Q7 204.3 mm to (165.5, 175.2)
- moved Q8 204.3 mm to (160.8, 180.5)
- moved R63 204.3 mm to (166.0, 184.6)
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- renumbered C115 to C1, C124 to C10, C131 to C105, C132 to C106, C133 to C107, C134 to C108, C135 to C109, C125 to C11, C136 to C110, C137 to C111, C177 to C112, C189 to C113, C138 to C114, C151 to C115, C150 to C116, C154 to C117, C156 to C118, C149 to C119, C126 to C12, C152 to C120, C153 to C121, C199 to C122, C200 to C123, C155 to C124, C157 to C125, C159 to C126, C160 to C127, C161 to C128, C162 to C129, C127 to C13, C163 to C130, C164 to C131, C165 to C132, C166 to C133, C167 to C134, C168 to C135, C169 to C136, C170 to C137, C171 to C138, C201 to C139, C128 to C14, C202 to C140, C176 to C141, C203 to C142, C204 to C143, C178 to C144, C174 to C145, C172 to C146, C188 to C147, C181 to C148, C182 to C149, C129 to C15, C179 to C150, C180 to C151, C184 to C152, C183 to C153, C185 to C154, C186 to C155, C187 to C156, C26 to C157, C205 to C158, C30 to C159, C139 to C16, C31 to C160, C206 to C161, C34 to C164, C60 to C167, C61 to C168, C140 to C17, C36 to C170, C37 to C171, C38 to C172, C39 to C173, C41 to C175, C42 to C176, C44 to C178, C25 to C18, C47 to C180, C48 to C181, C50 to C183, C52 to C185, C53 to C186, C55 to C188, C141 to C19, C58 to C190, C63 to C193, C66 to C196, C69 to C199, C116 to C2, C27 to C20, C71 to C201, C73 to C203, C74 to C204, C75 to C205, C76 to C206, C142 to C25, C148 to C26, C158 to C27, C173 to C29, C117 to C3, C29 to C30, C175 to C31, C197 to C32, C198 to C33, C114 to C34, C190 to C35, C191 to C36, C192 to C37, C193 to C38, C194 to C39, C118 to C4, C195 to C40, C196 to C41, C145 to C42, C119 to C5, C87 to C53, C89 to C55, C90 to C56, C92 to C58, C120 to C6, C95 to C61, C96 to C62, C97 to C63, C98 to C64, C99 to C65, C100 to C66, C101 to C67, C102 to C68, C103 to C69, C104 to C70, C105 to C71, C106 to C72, C107 to C73, C108 to C74, C109 to C75, C110 to C76, C111 to C77, C112 to C78, C113 to C79, C10 to C89, C11 to C90, C12 to C91, C13 to C92, C14 to C93, C18 to C97, D15 to D1, D17 to D10, D1 to D11, D2 to D12, D4 to D13, D20 to D16, D21 to D17, D27 to D19, D16 to D2, D23 to D21, D24 to D23, D25 to D24, D7 to D25, D9 to D26, D8 to D27, D10 to D28, D11 to D4, D12 to D5, D13 to D6, D14 to D7, D5 to D8, D6 to D9, FB4 to FB1, FB5 to FB2, FB1 to FB3, FB2 to FB4, FB3 to FB5, IC1 to IC2, J5 to J1, J2 to J10, J3 to J11, J8 to J4, J1 to J5, J9 to J6, J10 to J7, J7 to J9, N2 to N1, Q7 to Q10, Q5 to Q11, Q9 to Q3, Q1 to Q4, Q10 to Q5, Q11 to Q6, Q8 to Q7, Q2 to Q8, Q6 to Q9, R48 to R1, R57 to R10, R120 to R103, R121 to R104, R19 to R109, R58 to R11, R20 to R110, R21 to R111, R22 to R112, R25 to R115, R26 to R116, R125 to R118, R59 to R12, R127 to R120, R31 to R125, R32 to R126, R35 to R129, R61 to R14, R62 to R15, R63 to R16, R49 to R2, R65 to R20, R70 to R21, R74 to R22, R75 to R23, R16 to R24, R15 to R25, R12 to R26, R98 to R27, R99 to R28, R42 to R29, R50 to R3, R43 to R30, R45 to R32, R94 to R35, R95 to R36, R96 to R37, R97 to R38, R36 to R39, R51 to R4, R37 to R40, R38 to R41, R39 to R42, R40 to R43, R41 to R44, R83 to R45, R89 to R46, R1 to R47, R2 to R48, R52 to R5, R5 to R50, R6 to R51, R7 to R52, R9 to R54, R10 to R55, R11 to R56, R103 to R57, R104 to R58, R105 to R59, R53 to R6, R106 to R60, R93 to R61, R101 to R62, R107 to R63, R100 to R64, R108 to R65, R102 to R66, R109 to R67, R92 to R68, R110 to R69, R54 to R7, R91 to R70, R90 to R71, R88 to R72, R67 to R73, R111 to R74, R68 to R75, R69 to R76, R71 to R77, R112 to R78, R113 to R79, R55 to R8, R114 to R80, R115 to R81, R116 to R82, R80 to R83, R81 to R84, R72 to R85, R73 to R86, R82 to R87, R76 to R88, R77 to R89, R56 to R9, R78 to R90, R86 to R91, R79 to R92, R87 to R93, R117 to R94, R84 to R95, R85 to R96, R13 to R97, R14 to R98, U41 to U10, U42 to U11, U44 to U13, U16 to U15, U17 to U16, U18 to U17, U19 to U18, U20 to U19, U21 to U20, U1 to U21, U31 to U22, U32 to U23, U30 to U25, U34 to U26, U33 to U27, U47 to U28, U48 to U29, U26 to U3, U23 to U30, U35 to U31, U36 to U34, U37 to U35, U40 to U36, U4 to U39, U27 to U4, U5 to U40, U7 to U42, U13 to U47, U14 to U48, U28 to U5, U2 to U6, U45 to U7, U46 to U8, U22 to U9, Y5 to Y1, Y3 to Y2, Y4 to Y3, Y1 to Y4, Y2 to Y5
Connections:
- net Net-(C44-Pad1) renamed /Power Supply/DC/DC conventers/SW_PS_1V0
- C43 pad 2: Net-(C77-Pad2) -> GND
- C44 pad 2: Net-(C78-Pad2) -> GND
- C45 pad 1: /Power Supply/DC/DC conventers/DC_MAIN_BUS -> PS_3V3
- C46 pad 2: Net-(C78-Pad2) -> GND
- C48 pad 2: Net-(C78-Pad2) -> GND
- C49 pad 2: Net-(C77-Pad2) -> GND
- C50 pad 2: Net-(C78-Pad2) -> GND
- C51 pad 2: Net-(C78-Pad2) -> GND
- C52 pad 2: Net-(C77-Pad2) -> GND
- C54 pad 2: Net-(C78-Pad2) -> GND
- C57 pad 2: Net-(C78-Pad2) -> GND
- C59 pad 2: Net-(C78-Pad2) -> GND
- C60 pad 2: Net-(C78-Pad2) -> GND
- C8 pad 1: PS_2V5 -> PS_3V3
- D18 pad 2: GND -> Net-(D18-Pad2)
- D22 pad 2: GND -> Net-(D22-Pad2)
- J_SOM240_1 pad A59: /Xilinx K26 SOM/VCC_SOM -> SOM_5V
- J_SOM240_1 pad A60: /Xilinx K26 SOM/VCC_SOM -> SOM_5V
- J_SOM240_1 pad B37: /Xilinx K26 SOM/MIO51 -> /SD 3.0 card/MIO51
- J_SOM240_1 pad B60: /Xilinx K26 SOM/VCC_SOM -> SOM_5V
- J_SOM240_1 pad C59: /Xilinx K26 SOM/VCC_SOM -> SOM_5V
- J_SOM240_1 pad C60: /Xilinx K26 SOM/VCC_SOM -> SOM_5V
- J_SOM240_1 pad D60: /Xilinx K26 SOM/VCC_SOM -> SOM_5V
- L6 pad 1: Net-(C62-Pad1) -> Net-(C192-Pad1)
- Q12 pad 1: Net-(Q12-Pad1) -> PS_1V2
- Q12 pad 3: Net-(D26-Pad2) -> Net-(D18-Pad2)
- Q13 pad 1: Net-(Q13-Pad1) -> PS_1V0
- Q14 pad 1: Net-(Q14-Pad1) -> PL_1V2
- Q14 pad 3: Net-(D28-Pad2) -> Net-(D22-Pad2)
- R119 pad 1: PS_3V3 -> PL_3V3
- R122 pad 1: PS_1V2 -> PL_3V3
- R122 pad 2: Net-(Q12-Pad1) -> Net-(D22-Pad1)
- R123 pad 1: PS_3V3 -> PL_3V3
- R123 pad 2: Net-(D26-Pad1) -> Net-(R123-Pad2)
- R124 pad 1: PS_1V0 -> Net-(R123-Pad2)
- R124 pad 2: Net-(Q13-Pad1) -> GND
- R128 pad 1: PL_1V2 -> Net-(R127-Pad2)
- R128 pad 2: Net-(Q14-Pad1) -> GND
- R17 pad 1: PS_3V3 -> /SD 3.0 card/MIO46
- R33 pad 1: PL_1V2 -> PL_3V3
- R33 pad 2: Net-(R33-Pad2) -> /Camera interface/CCI0_I2C_SDA_3V3
- R34 pad 1: Net-(R33-Pad2) -> PL_3V3
- R34 pad 2: GND -> /Camera interface/CCI1_I2C_SDA_3V3
- U12 pad 1: /Power Supply/PoE/POE_12V -> /PMOD/HDA11
- U12 pad 10: Net-(U12-Pad10) -> /PMOD/HDA11
- U12 pad 2: /Power Supply/PoE/POE_12V -> /PMOD/HDA12
- U12 pad 3: /Power Supply/PoE/POE_12V -> GND
- U12 pad 4: /Power Supply/PoE/POE_12V -> /PMOD/HDA13
- U12 pad 5: Net-(U12-Pad5) -> /PMOD/HDA14
- U12 pad 6: Net-(U12-Pad6) -> /PMOD/HDA14
- U12 pad 7: GND -> /PMOD/HDA13
- U12 pad 8: /Power Supply/DC/DC conventers/DC_MAIN_BUS -> GND
- U12 pad 9: /Power Supply/DC/DC conventers/DC_MAIN_BUS -> /PMOD/HDA12
- U4 pad 3: Net-(R64-Pad8) -> Net-(R17-Pad2)
- U43 pad 1: /PMOD/HDA11 -> GND
- U43 pad 2: /PMOD/HDA12 -> Net-(C192-Pad1)
- U43 pad 3: GND -> /Power Supply/DC/DC conventers/DC_MAIN_BUS
- U43 pad 4: /PMOD/HDA13 -> Net-(R123-Pad2)
- U43 pad 5: /PMOD/HDA14 -> /Power Supply/VCCOEN_PS_M2C
- U43 pad 6: /PMOD/HDA14 -> Net-(C192-Pad2)
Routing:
- net PS_1V0: track 0.00 -> 8.09 mm, vias 0 -> 10
- net Net-(D26-Pad2): track 5.46 -> 0.00 mm
- net Net-(D19-Pad2): track 0.00 -> 5.12 mm
- net Net-(J5-Pad7): track 0.00 -> 3.66 mm
- net Net-(J5-Pad8): track 0.00 -> 3.15 mm
- net Net-(R115-Pad2): track 0.00 -> 2.19 mm
- net PS_1V8: track 0.00 -> 1.94 mm, vias 0 -> 1
- net SOM_5V: track 0.00 -> 1.71 mm, vias 0 -> 3
- net /Xilinx K26 SOM/VCC_SOM: track 1.71 -> 0.00 mm, vias 3 -> 0
- net Net-(D18-Pad2): track 0.00 -> 1.31 mm
- net GND: track 3.53 -> 4.83 mm, vias 6 -> 16
- net Net-(Q12-Pad1): track 1.25 -> 0.00 mm
- net /Power Supply/VCCOEN_PL_M2C: track 0.00 -> 1.20 mm, vias 0 -> 1
- net Net-(C178-Pad2): track 0.00 -> 1.09 mm
- net Net-(D26-Pad1): track 1.06 -> 0.00 mm
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- added copper zone on F.Cu, net /Power Supply/DC/DC conventers/DC_MAIN_BUS
- added copper zone on F.Cu, net /Power Supply/DC/DC conventers/SW_PS_1V0
- added copper zone on F.Cu, net GND
- added copper zone on F.Cu, net PS_1V0
